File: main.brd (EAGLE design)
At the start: 35.6 x 47 mm, 12 parts

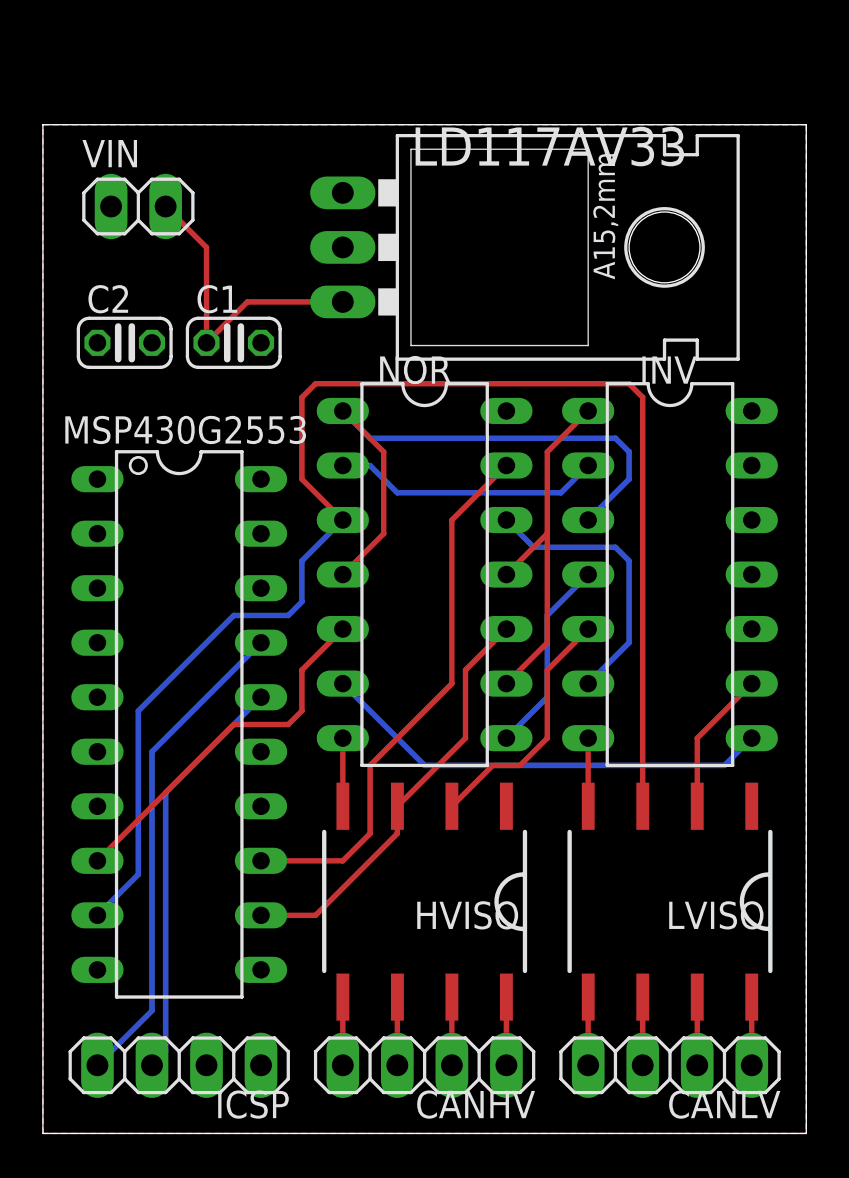
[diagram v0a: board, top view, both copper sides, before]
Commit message: Added pin annotations
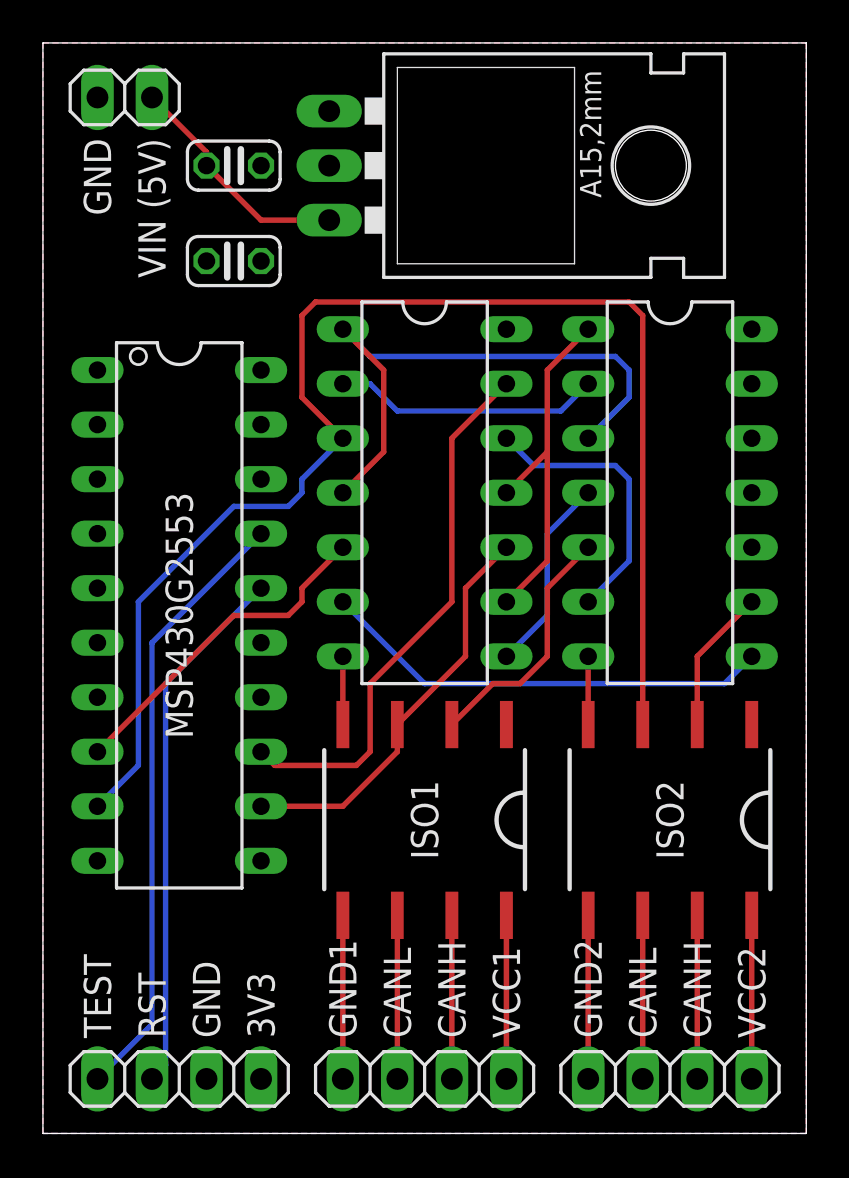
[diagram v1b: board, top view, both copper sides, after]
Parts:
- removed CANHV, CANLV: (no value), pinhead:1X04
- removed HVISO, LVISO: (no value), texas:DUB-R-PDSO-G8
- added CAN1, CAN2: (no value), pinhead:1X04
- added ISO1, ISO2: (no value), texas:DUB-R-PDSO-G8
- moved C1 8.26 mm to (8.89, 45.1)
- moved C2 6.35 mm to (8.89, 40.6)
- moved VIN 5.12 mm to (3.81, 48.3)
- moved MSP430G2553 5.08 mm to (6.35, 24.1)
- moved LD117AV33 3.86 mm to (17.1, 45.1)
- moved INV 3.81 mm to (29.2, 29.8)
- moved NOR 3.81 mm to (17.8, 29.8)
- moved ICSP 0.63 mm to (6.35, 2.54)
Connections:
- net GND: now also ISO1.4, ISO2.4; no longer HVISO.4, LVISO.4
- net N$10: now also CAN2.2, ISO2.7; no longer CANLV.2, LVISO.7
- net N$11: now also CAN2.3, ISO2.6; no longer CANLV.3, LVISO.6
- net N$12: now also CAN2.4, ISO2.5; no longer CANLV.4, LVISO.5
- net N$13: now also CAN1.1, ISO1.8; no longer CANHV.1, HVISO.8
- net N$14: now also CAN1.2, ISO1.7; no longer CANHV.2, HVISO.7
- net N$15: now also CAN1.3, ISO1.6; no longer CANHV.3, HVISO.6
- net N$16: now also CAN1.4, ISO1.5; no longer CANHV.4, HVISO.5
- net N$18: now also ISO1.2; no longer HVISO.2
- net N$20: now also ISO2.2; no longer LVISO.2
- net N$24: now also ISO2.3; no longer LVISO.3
- net N$25: now also ISO1.3; no longer HVISO.3
- net N$9: now also CAN2.1, ISO2.8; no longer CANLV.1, LVISO.8
- net VCC: now also ISO1.1, ISO2.1; no longer HVISO.1, LVISO.1
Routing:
- net N$2: track 22.8 -> 28.6 mm
- net N$1: track 19.2 -> 25.0 mm
- net N$9: track 3.17 -> 7.62 mm
- net N$16: track 3.17 -> 7.62 mm
- net N$15: track 3.17 -> 7.62 mm
- net N$14: track 3.17 -> 7.62 mm
- net N$13: track 3.17 -> 7.62 mm
- net N$12: track 3.17 -> 7.62 mm
- net N$11: track 3.17 -> 7.62 mm
- net N$10: track 3.17 -> 7.62 mm
- net N$23: track 14.3 -> 11.0 mm
- net N$21: track 17.0 -> 15.7 mm
- net N$24: track 66.6 -> 65.3 mm
- net N$25: track 19.6 -> 19.0 mm
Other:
- board size 35.6 x 47 mm -> 35.6 x 50.8 mm
- board text added: "3V3"
- board text added: "CANH"
- board text added: "CANL"
- board text added: "GND"
- board text added: "GND1"
- board text added: "GND2"
- board text added: "ISO1"
- board text added: "ISO2"
- board text added: "RST"
- board text added: "TEST"
- board text added: "VCC1"
- board text added: "VCC2"
- board text added: "VIN (5V)"
